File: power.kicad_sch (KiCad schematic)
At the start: 13 parts, among them U20 power_conn_10, U21 REF191, U22 L78L05ACU, U23 ZLDO1117G33TA, U24 TL072

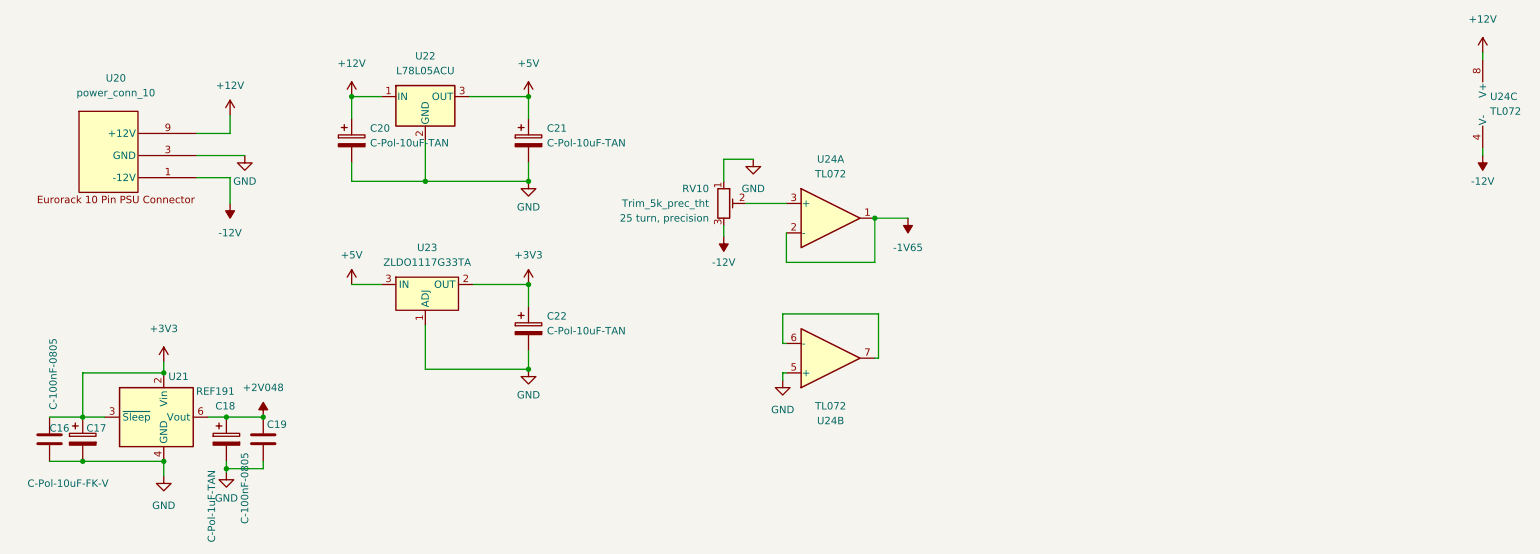
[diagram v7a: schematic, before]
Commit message: reannotated changed to LM324
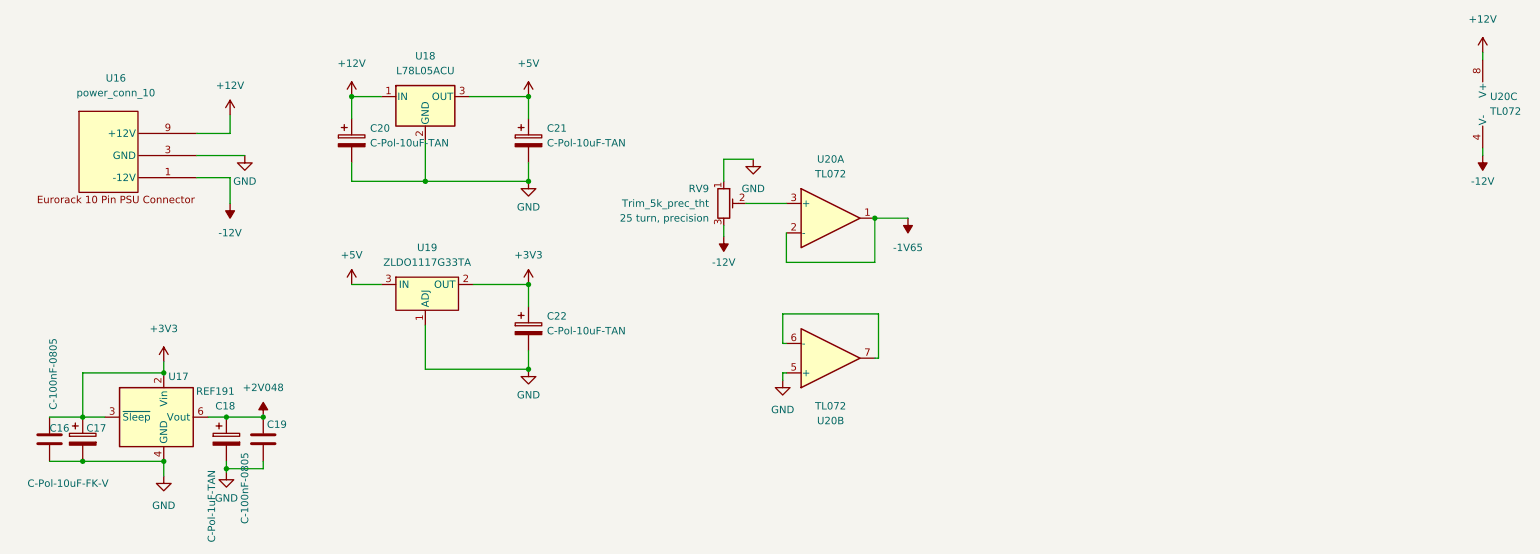
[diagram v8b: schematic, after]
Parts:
- renumbered RV10 to RV9, U20 to U16, U21 to U17, U22 to U18, U23 to U19, U24 to U20
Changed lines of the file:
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@@
   (symbol (lib_id "eurorack:power_conn_10") (at 37.465 32.385 0) (unit 1)
     (in_bom yes) (on_board yes) (fields_autoplaced)
-    (property "Reference" "U20" (id 0) (at 38.735 25.4 0))
+    (property "Reference" "U16" (id 0) (at 38.735 25.4 0))
     (property "Value" "power_conn_10" (id 1) (at 38.735 27.94 0))
     (property "Footprint" "eurorack:power_10" (id 2) (at 40.005 48.895 0)
@@
   (symbol (lib_id "power:-12V") (at 143.51 52.705 180) (unit 1)
     (in_bom yes) (on_board yes) (fields_autoplaced)
-    (property "Reference" "#PWR0111" (id 0) (at 143.51 55.245 0)
+    (property "Reference" "#PWR087" (id 0) (at 143.51 55.245 0)
       (effects (font (size 1.27 1.27)) hide)
     )
@@
   (symbol (lib_id "power:+12V") (at 79.375 28.575 0) (unit 1)
     (in_bom yes) (on_board yes) (fields_autoplaced)
-    (property "Reference" "#PWR0105" (id 0) (at 79.375 32.385 0)
+    (property "Reference" "#PWR081" (id 0) (at 79.375 32.385 0)
       (effects (font (size 1.27 1.27)) hide)
     )
@@
   (symbol (lib_id "power:GND") (at 109.855 75.565 0) (unit 1)
     (in_bom yes) (on_board yes) (fields_autoplaced)
-    (property "Reference" "#PWR0110" (id 0) (at 109.855 81.915 0)
+    (property "Reference" "#PWR086" (id 0) (at 109.855 81.915 0)
       (effects (font (size 1.27 1.27)) hide)
     )
@@
   (symbol (lib_id "eurorack:Trim_5k_prec_tht") (at 143.51 46.99 0) (unit 1)
     (in_bom yes) (on_board yes) (fields_autoplaced)
-    (property "Reference" "RV10" (id 0) (at 140.97 44.4499 0)
+    (property "Reference" "RV9" (id 0) (at 140.97 44.4499 0)
       (effects (font (size 1.27 1.27)) (justify right))
     )
@@
   (symbol (lib_id "power:+5V") (at 79.375 60.96 0) (unit 1)
     (in_bom yes) (on_board yes) (fields_autoplaced)
-    (property "Reference" "#PWR0106" (id 0) (at 79.375 64.77 0)
+    (property "Reference" "#PWR082" (id 0) (at 79.375 64.77 0)
       (effects (font (size 1.27 1.27)) hide)
     )
@@
   (symbol (lib_id "power:GND") (at 46.99 93.98 0) (unit 1)
     (in_bom yes) (on_board yes) (fields_autoplaced)
-    (property "Reference" "#PWR099" (id 0) (at 46.99 100.33 0)
+    (property "Reference" "#PWR075" (id 0) (at 46.99 100.33 0)
       (effects (font (size 1.27 1.27)) hide)
     )
@@
   (symbol (lib_id "power:-12V") (at 274.32 38.735 180) (unit 1)
     (in_bom yes) (on_board yes) (fields_autoplaced)
-    (property "Reference" "#PWR0116" (id 0) (at 274.32 41.275 0)
+    (property "Reference" "#PWR092" (id 0) (at 274.32 41.275 0)
       (effects (font (size 1.27 1.27)) hide)
     )
@@
   (symbol (lib_id "eurorack:L78L05ACU") (at 92.075 28.575 0) (unit 1)
     (in_bom yes) (on_board yes) (fields_autoplaced)
-    (property "Reference" "U22" (id 0) (at 92.075 21.59 0))
+    (property "Reference" "U18" (id 0) (at 92.075 21.59 0))
     (property "Value" "L78L05ACU" (id 1) (at 92.075 24.13 0))
     (property "Footprint" "Package_TO_SOT_SMD:SOT-89-3_Handsoldering" (id 2) (at 92.71 32.385 0)
@@
   (symbol (lib_id "power:GND") (at 57.785 93.345 0) (unit 1)
     (in_bom yes) (on_board yes) (fields_autoplaced)
-    (property "Reference" "#PWR0100" (id 0) (at 57.785 99.695 0)
+    (property "Reference" "#PWR076" (id 0) (at 57.785 99.695 0)
       (effects (font (size 1.27 1.27)) hide)
     )
@@
   (symbol (lib_id "eurorack:TL072") (at 161.925 49.53 0) (unit 1)
     (in_bom yes) (on_board yes) (fields_autoplaced)
-    (property "Reference" "U24" (id 0) (at 161.925 39.37 0))
+    (property "Reference" "U20" (id 0) (at 161.925 39.37 0))
     (property "Value" "TL072" (id 1) (at 161.925 41.91 0))
     (property "Footprint" "Package_SO:SO-8_3.9x4.9mm_P1.27mm" (id 2) (at 161.925 49.53 0)
@@
   (symbol (lib_id "power:+5V") (at 109.855 28.575 0) (unit 1)
     (in_bom yes) (on_board yes) (fields_autoplaced)
-    (property "Reference" "#PWR0107" (id 0) (at 109.855 32.385 0)
+    (property "Reference" "#PWR083" (id 0) (at 109.855 32.385 0)
       (effects (font (size 1.27 1.27)) hide)
     )
@@
   (symbol (lib_id "eurorack:ZLDO1117G33TA") (at 92.075 58.42 0) (unit 1)
     (in_bom yes) (on_board yes) (fields_autoplaced)
-    (property "Reference" "U23" (id 0) (at 92.3925 54.61 0))
+    (property "Reference" "U19" (id 0) (at 92.3925 54.61 0))
     (property "Value" "ZLDO1117G33TA" (id 1) (at 92.3925 57.15 0))
     (property "Footprint" "Package_TO_SOT_SMD:SOT-223" (id 2) (at 92.075 58.42 0)
@@
   (symbol (lib_id "power:+3V3") (at 109.855 60.96 0) (unit 1)
     (in_bom yes) (on_board yes) (fields_autoplaced)
-    (property "Reference" "#PWR0109" (id 0) (at 109.855 64.77 0)
+    (property "Reference" "#PWR085" (id 0) (at 109.855 64.77 0)
       (effects (font (size 1.27 1.27)) hide)
     )
@@
   (symbol (lib_id "power:GND") (at 60.96 38.735 0) (unit 1)
     (in_bom yes) (on_board yes) (fields_autoplaced)
-    (property "Reference" "#PWR0103" (id 0) (at 60.96 45.085 0)
+    (property "Reference" "#PWR079" (id 0) (at 60.96 45.085 0)
       (effects (font (size 1.27 1.27)) hide)
     )
@@
   (symbol (lib_id "power:+3V3") (at 46.99 74.295 0) (unit 1)
     (in_bom yes) (on_board yes) (fields_autoplaced)
-    (property "Reference" "#PWR098" (id 0) (at 46.99 78.105 0)
+    (property "Reference" "#PWR074" (id 0) (at 46.99 78.105 0)
       (effects (font (size 1.27 1.27)) hide)
     )
@@
   (symbol (lib_id "eurorack:TL072") (at 161.925 73.66 0) (mirror x) (unit 2)
     (in_bom yes) (on_board yes) (fields_autoplaced)
-    (property "Reference" "U24" (id 0) (at 161.925 84.455 0))
+    (property "Reference" "U20" (id 0) (at 161.925 84.455 0))
     (property "Value" "TL072" (id 1) (at 161.925 81.915 0))
     (property "Footprint" "Package_SO:SO-8_3.9x4.9mm_P1.27mm" (id 2) (at 161.925 73.66 0)
@@
   (symbol (lib_id "eurorack:REF191") (at 46.99 83.82 0) (unit 1)
     (in_bom yes) (on_board yes)
-    (property "Reference" "U21" (id 0) (at 49.53 76.835 0))
+    (property "Reference" "U17" (id 0) (at 49.53 76.835 0))
     (property "Value" "REF191" (id 1) (at 55.88 79.375 0))
     (property "Footprint" "Package_SO:SO-8_3.9x4.9mm_P1.27mm" (id 2) (at 46.99 85.09 0)
@@
   (symbol (lib_id "power:GND") (at 109.855 43.18 0) (unit 1)
     (in_bom yes) (on_board yes) (fields_autoplaced)
-    (property "Reference" "#PWR0108" (id 0) (at 109.855 49.53 0)
+    (property "Reference" "#PWR084" (id 0) (at 109.855 49.53 0)
       (effects (font (size 1.27 1.27)) hide)
     )
@@
   (symbol (lib_id "power:+12V") (at 274.32 20.955 0) (unit 1)
     (in_bom yes) (on_board yes) (fields_autoplaced)
-    (property "Reference" "#PWR0115" (id 0) (at 274.32 24.765 0)
+    (property "Reference" "#PWR091" (id 0) (at 274.32 24.765 0)
       (effects (font (size 1.27 1.27)) hide)
     )
@@
   (symbol (lib_id "power:GND") (at 148.59 39.37 0) (unit 1)
     (in_bom yes) (on_board yes) (fields_autoplaced)
-    (property "Reference" "#PWR0112" (id 0) (at 148.59 45.72 0)
+    (property "Reference" "#PWR088" (id 0) (at 148.59 45.72 0)
       (effects (font (size 1.27 1.27)) hide)
     )
@@
   (symbol (lib_id "power:+12V") (at 58.42 31.75 0) (unit 1)
     (in_bom yes) (on_board yes) (fields_autoplaced)
-    (property "Reference" "#PWR0101" (id 0) (at 58.42 35.56 0)
+    (property "Reference" "#PWR077" (id 0) (at 58.42 35.56 0)
       (effects (font (size 1.27 1.27)) hide)
     )
@@
   (symbol (lib_id "power:GND") (at 153.67 77.47 0) (mirror y) (unit 1)
     (in_bom yes) (on_board yes) (fields_autoplaced)
-    (property "Reference" "#PWR0113" (id 0) (at 153.67 83.82 0)
+    (property "Reference" "#PWR089" (id 0) (at 153.67 83.82 0)
       (effects (font (size 1.27 1.27)) hide)
     )
@@
   (symbol (lib_id "power:-12V") (at 58.42 46.99 180) (unit 1)
     (in_bom yes) (on_board yes) (fields_autoplaced)
-    (property "Reference" "#PWR0102" (id 0) (at 58.42 49.53 0)
+    (property "Reference" "#PWR078" (id 0) (at 58.42 49.53 0)
       (effects (font (size 1.27 1.27)) hide)
     )
@@
   (symbol (lib_id "eurorack:TL072") (at 276.86 29.845 0) (unit 3)
     (in_bom yes) (on_board yes) (fields_autoplaced)
-    (property "Reference" "U24" (id 0) (at 275.59 28.5749 0)
+    (property "Reference" "U20" (id 0) (at 275.59 28.5749 0)
       (effects (font (size 1.27 1.27)) (justify left))
     )
@@
   (symbol (lib_id "eurorack:-1V65") (at 175.26 49.53 180) (unit 1)
     (in_bom yes) (on_board yes) (fields_autoplaced)
-    (property "Reference" "#PWR0114" (id 0) (at 175.26 52.07 0)
+    (property "Reference" "#PWR090" (id 0) (at 175.26 52.07 0)
       (effects (font (size 1.27 1.27)) hide)
     )
@@
   (symbol (lib_id "eurorack:+2V048") (at 64.135 83.82 0) (unit 1)
     (in_bom yes) (on_board yes) (fields_autoplaced)
-    (property "Reference" "#PWR0104" (id 0) (at 64.135 81.28 0)
-      (effects (font (size 1.27 1.27)) hide)
-    )
+    (property "Reference" "#PWR080" (id 0) (at 64.135 81.28 0)
+      (effects (font (size 1.27 1.27)) hide)
+    )
